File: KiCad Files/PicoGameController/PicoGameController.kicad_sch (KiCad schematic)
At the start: 59 parts, among them J1 USB_OTG, J2 Conn_01x02, J3 AudioJack4, SW1 SW_SPST, SW10 SW_SPST, SW11 SW_SPST, SW12 SW_SPST, SW13 SW_SPST, SW2 SW_SPST, SW3 SW_SPST, SW4 SW_SPST, SW5 SW_SPST, SW6 SW_SPST, SW7 SW_SPST, SW8 SW_SPST, SW9 SW_SPST, T1 THB001P, T2 THB001P, U1 RP2040, U2 NCP1117-3.3_SOT223, U3 W25Q128JVS, U4 DRV2605LDGS, U5 DRV2605LDGS, U6 UDA1334ATS, U7 ADS1115IDGS, U8 ADS1115IDGS, Y1 ABLS-12.000MHZ-B4-T

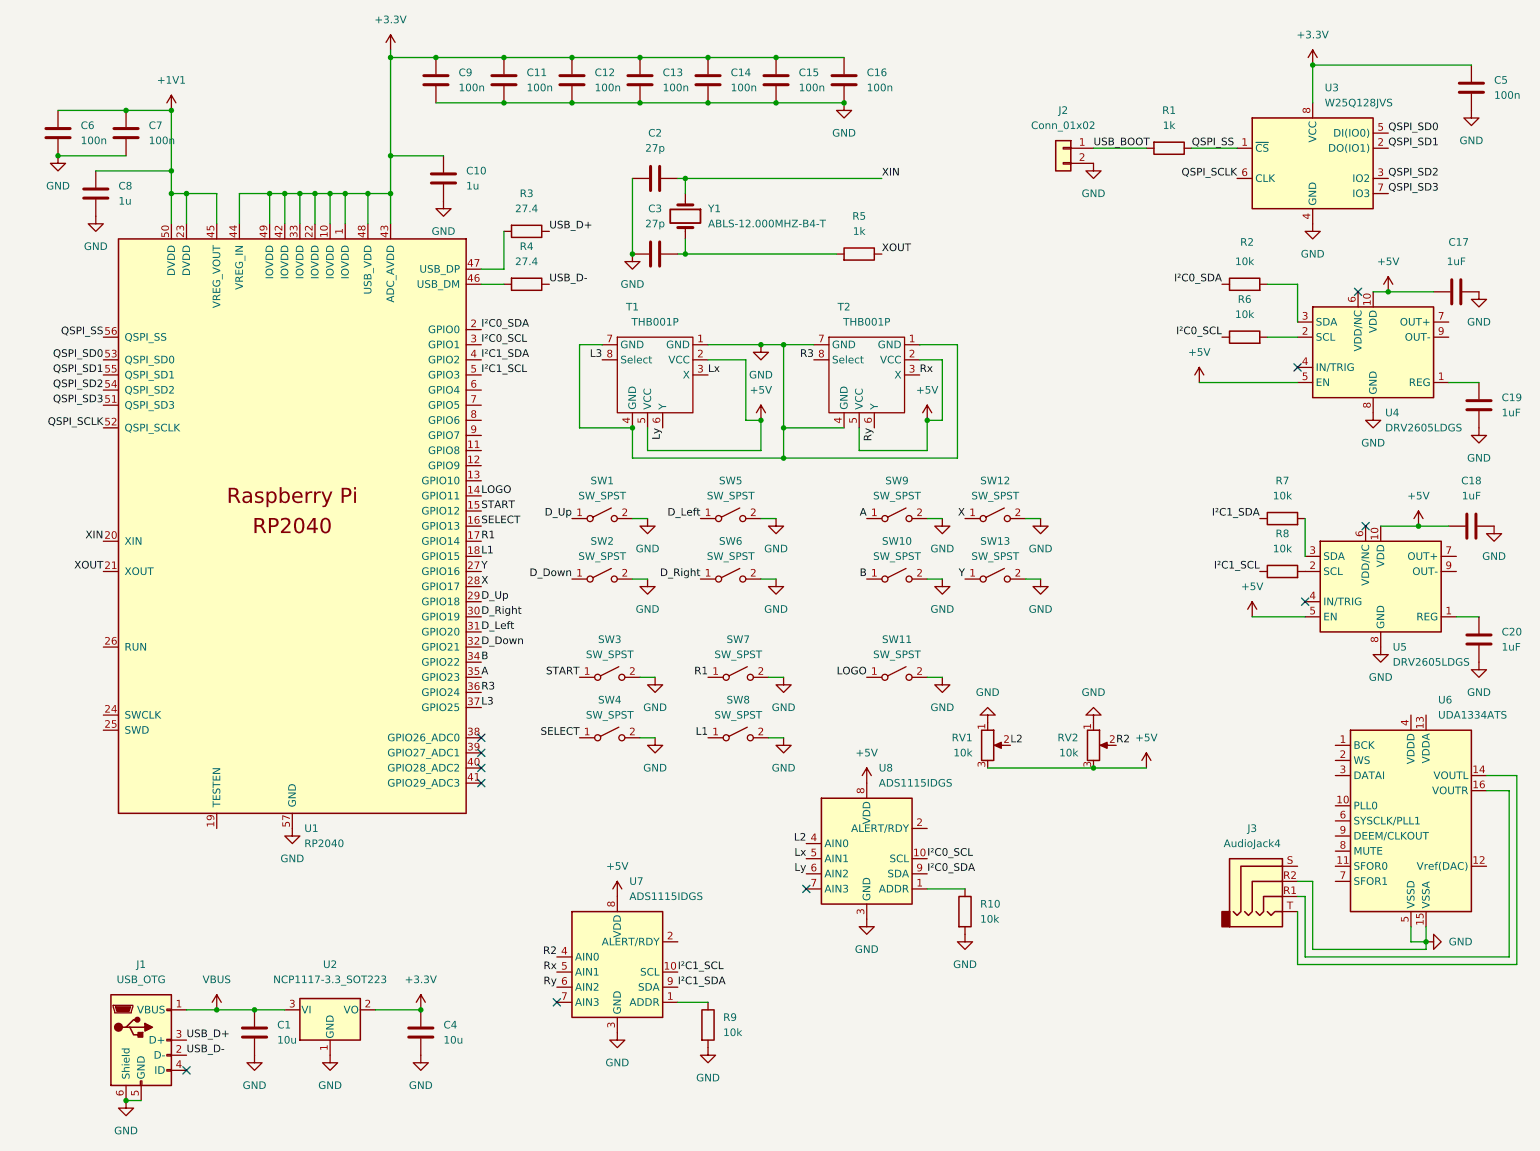
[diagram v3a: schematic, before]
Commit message: Redoing the buttons
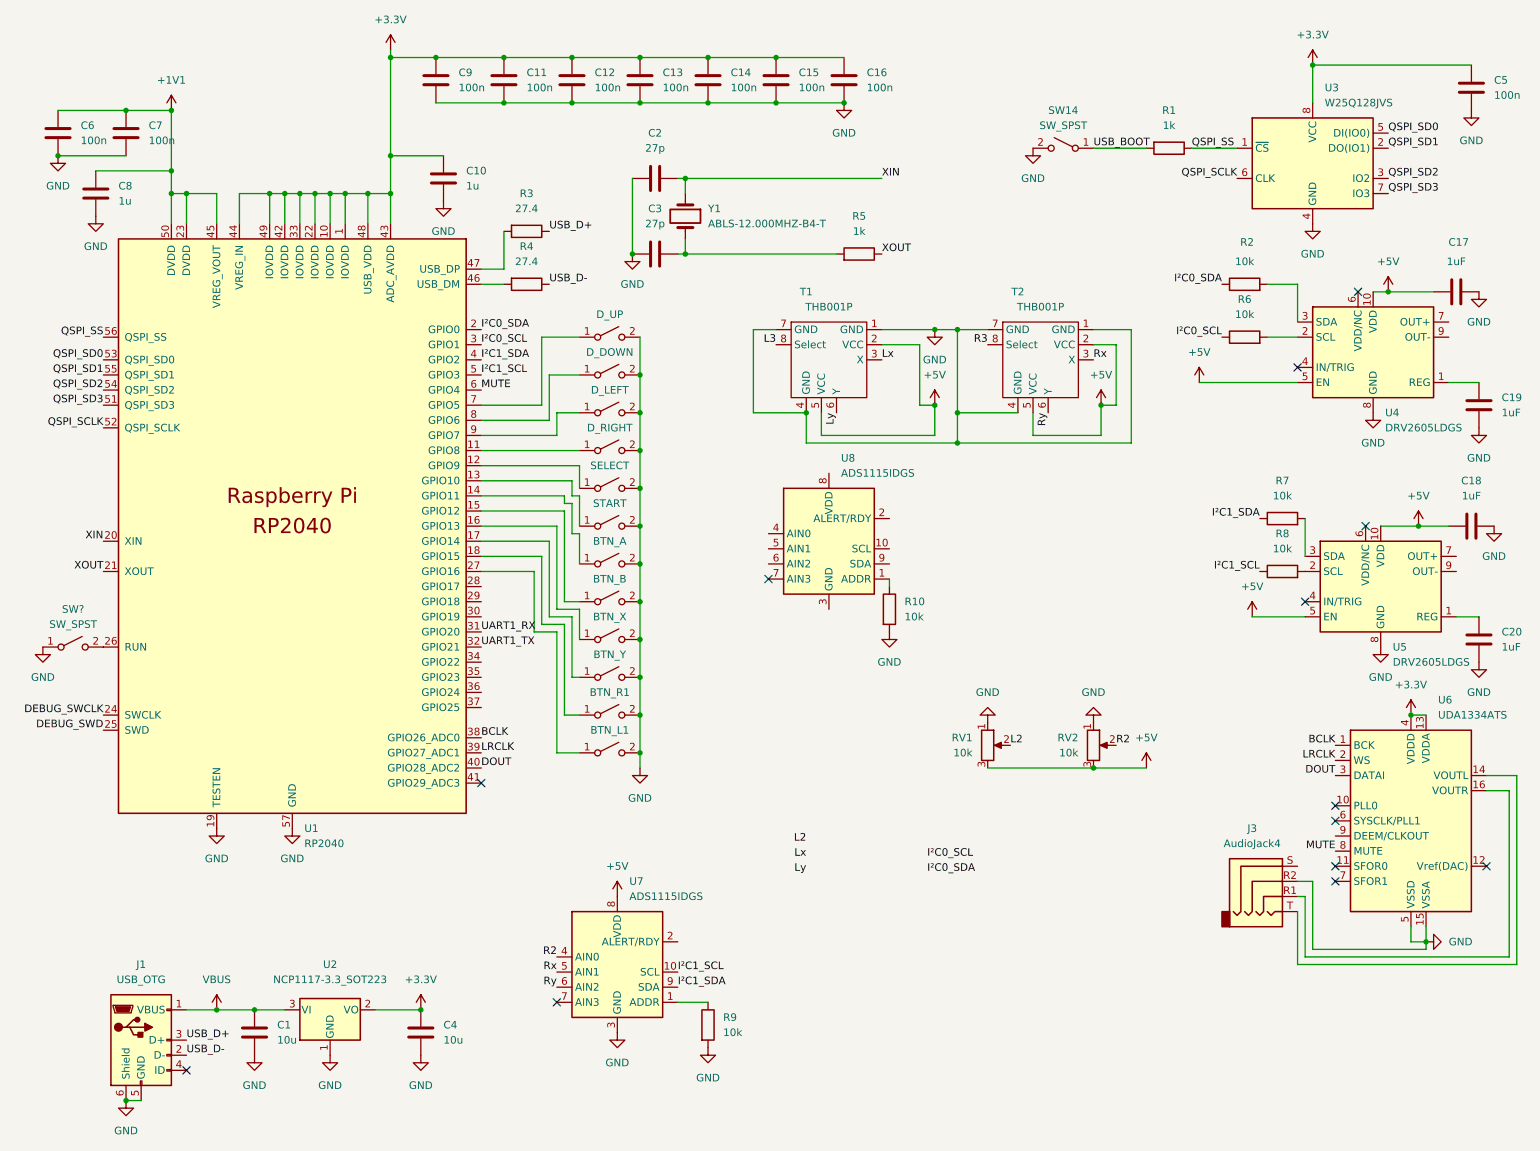
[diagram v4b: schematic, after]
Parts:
- removed J2: Conn_01x02, symbol Connector_Generic:Conn_01x02
- removed SW10, SW11, SW12, SW13, SW4, SW5, SW6, SW7, SW8, SW9: SW_SPST, symbol Switch:SW_SPST
- added BTN_A, BTN_B, BTN_L1, BTN_R1, BTN_X, BTN_Y, D_RIGHT, SELECT, START, SW14, SW?: SW_SPST, symbol Switch:SW_SPST
- renumbered SW2 to D_DOWN, SW3 to D_LEFT, SW1 to D_UP
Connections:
- net +3V3: now also U6.13 (VDDA), U6.4 (VDDD)
- net +5V: no longer U8.8 (VDD)
- net GND: now also U1.19 (TESTEN), BTN_A.2 (B), BTN_B.2 (B), BTN_L1.2 (B), BTN_R1.2 (B), BTN_X.2 (B), BTN_Y.2 (B), D_RIGHT.2 (B), SELECT.2 (B), START.2 (B), SW14.2 (B), SW?.1 (A); no longer U8.3 (GND)
- net I²C0_SCL: no longer U8.10 (SCL)
- net I²C0_SDA: no longer U8.9 (SDA)
- net L2: no longer U8.4 (AIN0)
- net L3: no longer U1.37 (GPIO25)
- net Lx: no longer U8.5 (AIN1)
- net Ly: no longer U8.6 (AIN2)
- net R3: no longer U1.36 (GPIO24)
- net USB_BOOT: now also SW14.1 (A)
- net at U1.11 (GPIO8): now also D_RIGHT.1 (A)
- net at U1.12 (GPIO9): now also SELECT.1 (A)
- net at U1.13 (GPIO10): now also START.1 (A)
- net DEBUG_SWCLK: now reaches U1.24 (SWCLK)
- net DEBUG_SWD: now reaches U1.25 (SWD)
- net at U1.26 (RUN): now also SW?.2 (B)
- net BCLK: now reaches U1.38 (GPIO26_ADC0)
- net BCLK: now also U6.1 (BCK)
- net LRCLK: now reaches U1.39 (GPIO27_ADC1)
- net LRCLK: now also U6.2 (WS)
- net DOUT: now reaches U1.40 (GPIO28_ADC2)
- net DOUT: now also U6.3 (DATAI)
- net MUTE: now reaches U1.6 (GPIO4)
- net MUTE: now also U6.8 (MUTE)
- net at U1.7 (GPIO5): now also D_UP.1 (A)
- net at U1.8 (GPIO6): now also D_DOWN.1 (A)
- net at U1.9 (GPIO7): now also D_LEFT.1 (A)
- net A: no longer names the net of U1.35 (GPIO23)
- net B: no longer names the net of U1.34 (GPIO22)
- net D_Down renamed UART1_TX
- net UART1_TX: no longer D_DOWN.1 (A)
- net D_Left renamed UART1_RX
- net D_Right: no longer names the net of U1.30 (GPIO19)
- net D_Up: no longer names the net of U1.29 (GPIO18)
- net D_Up: no longer D_UP.1 (A)
- net L1: no longer names the net of U1.18 (GPIO15)
- net L1: now also BTN_R1.1 (A)
- net LOGO: no longer names the net of U1.14 (GPIO11)
- net LOGO: now also BTN_A.1 (A)
- net R1: no longer names the net of U1.17 (GPIO14)
- net R1: now also BTN_Y.1 (A)
- net SELECT: no longer names the net of U1.16 (GPIO13)
- net SELECT: now also BTN_X.1 (A)
- net START: no longer names the net of U1.15 (GPIO12)
- net START: now also BTN_B.1 (A); no longer D_LEFT.1 (A)
- net X: no longer names the net of U1.28 (GPIO17)
- net Y: no longer names the net of U1.27 (GPIO16)
- net Y: now also BTN_L1.1 (A)
- no-connect marks 11 -> 13
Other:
- moved on the sheet: D_DOWN, D_LEFT, D_UP, R10, T1, T2, U8

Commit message: Adding hierarchel sheets
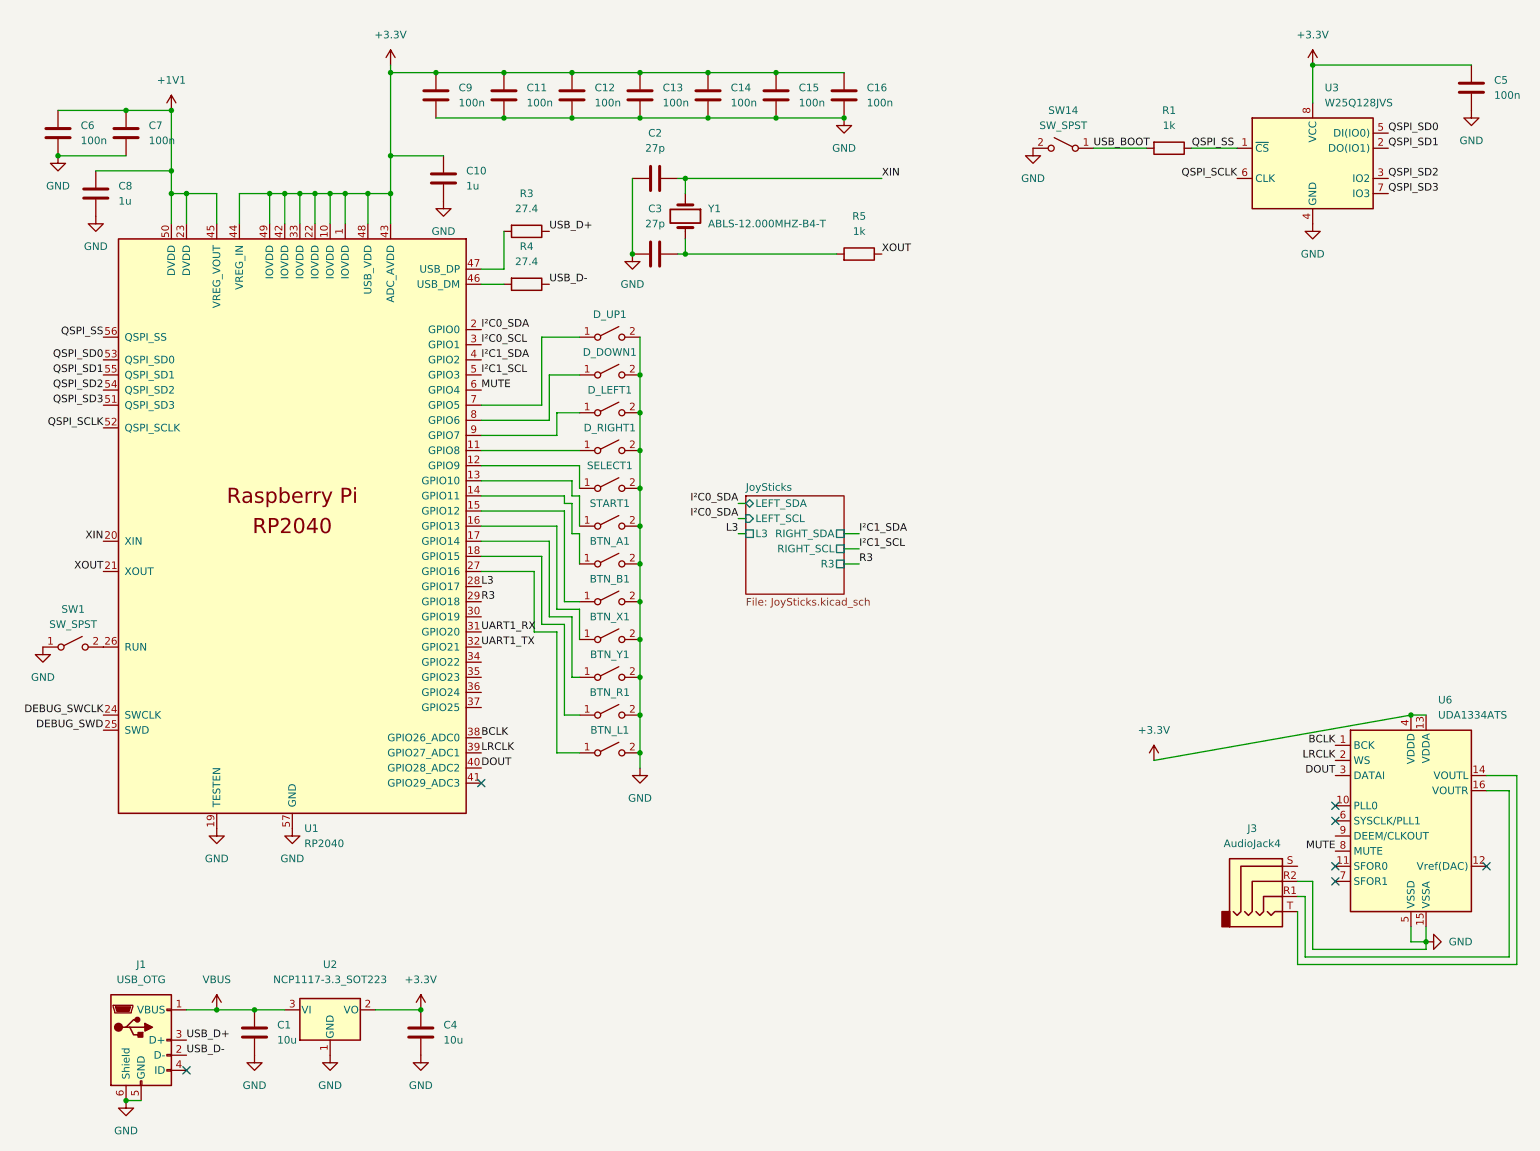
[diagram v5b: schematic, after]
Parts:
- removed C17, C18, C19, C20: 1uF, Capacitor_SMD:C_0201_0603Metric, symbol Device:C
- removed R10, R2, R6, R7, R8, R9: 10k, Resistor_SMD:R_0201_0603Metric, symbol Device:R
- removed RV1, RV2: 10k, Resistor_SMD:R_0201_0603Metric, symbol Device:R_Potentiometer
- removed T1, T2: THB001P, symbol CustomParts:THB001P
- removed U4, U5: DRV2605LDGS, Package_SO:VSSOP-10_3x3mm_P0.5mm, symbol Driver_Haptic:DRV2605LDGS
- removed U7, U8: ADS1115IDGS, Package_SO:TSSOP-10_3x3mm_P0.5mm, symbol Analog_ADC:ADS1115IDGS
- gave numbers to parts that had none: 1
- renumbered BTN_A to BTN_A1, BTN_B to BTN_B1, BTN_X to BTN_X1, BTN_Y to BTN_Y1, D_DOWN to D_DOWN1, D_LEFT to D_LEFT1, D_RIGHT to D_RIGHT1, D_UP to D_UP1, SELECT to SELECT1, START to START1
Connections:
- net L3: now also U1.28 (GPIO17)
- net R3: now also U1.29 (GPIO18)
- no-connect marks 13 -> 7
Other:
- added sheet JoySticks (JoySticks.kicad_sch)
- moved on the sheet: C11, C12, C13, C14, C15, C16, C9
